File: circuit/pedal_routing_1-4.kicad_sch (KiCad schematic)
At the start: 12 parts, among them U501 CD4051B, U502 CD4051B, U503 CD4051B, U504 CD4051B

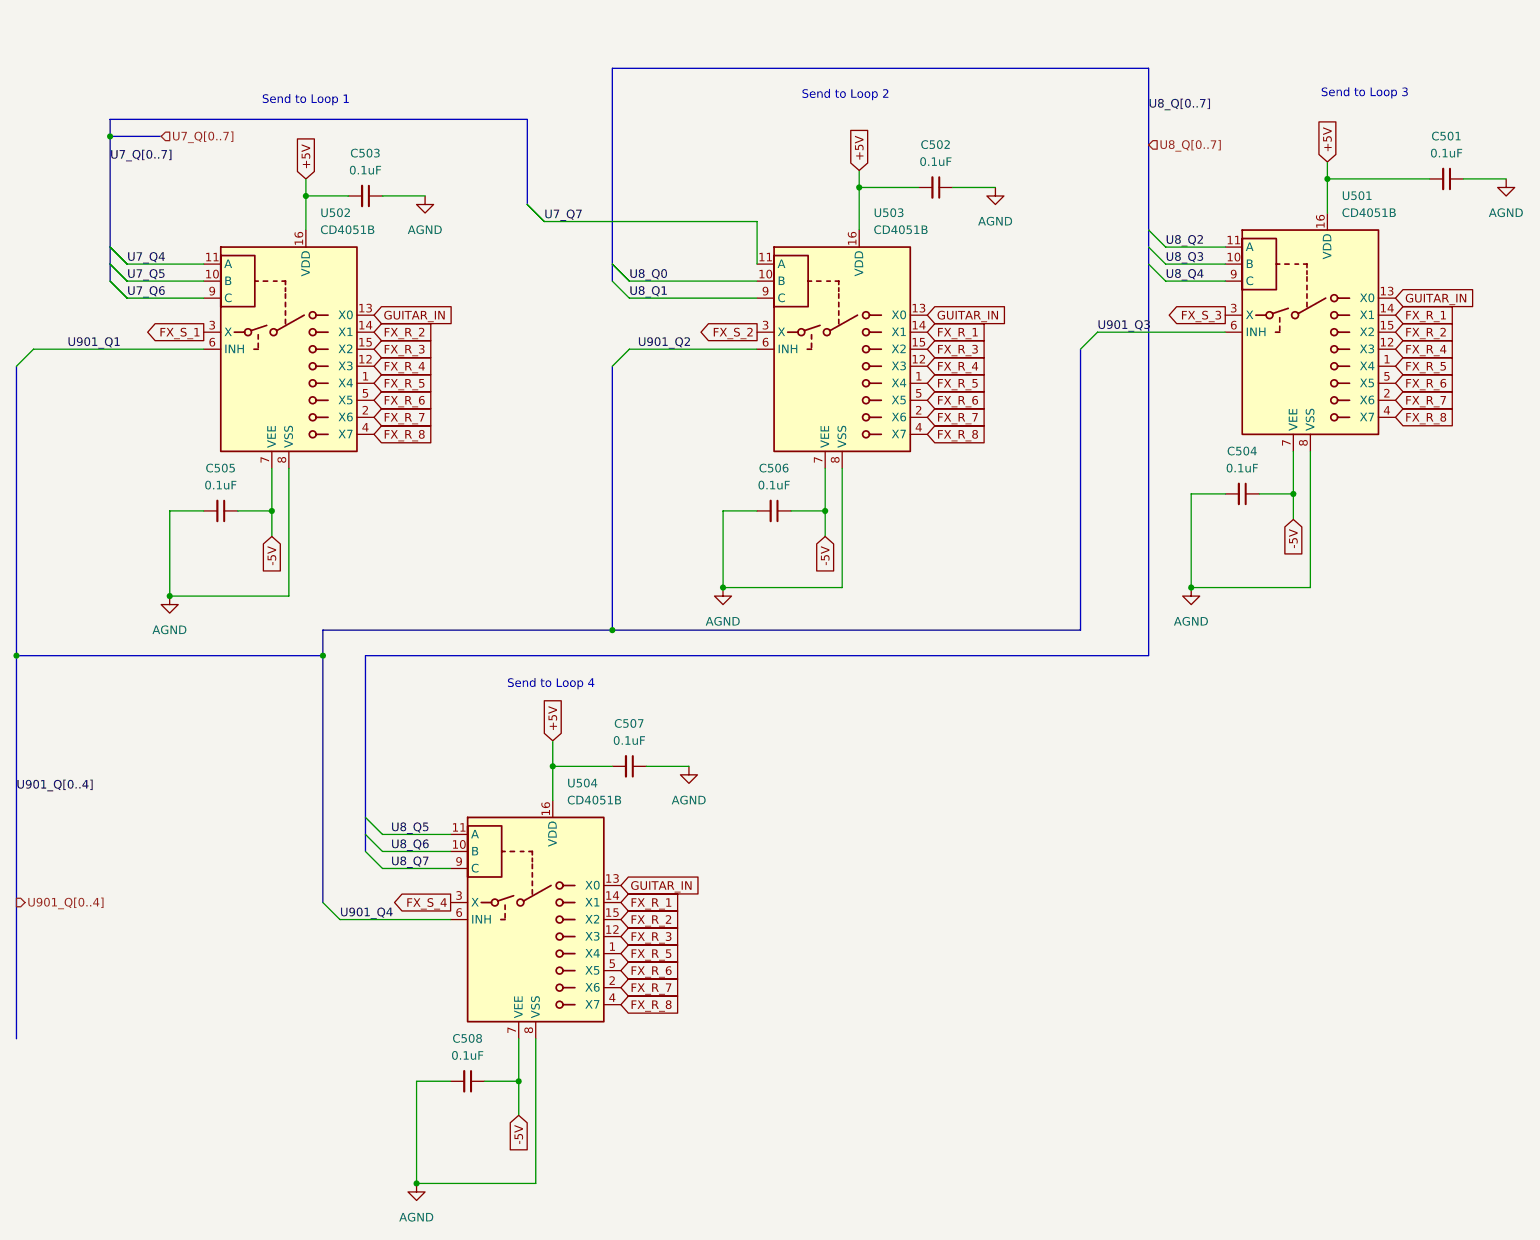
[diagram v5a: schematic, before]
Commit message: Added ferrite beads and tweaked PCB
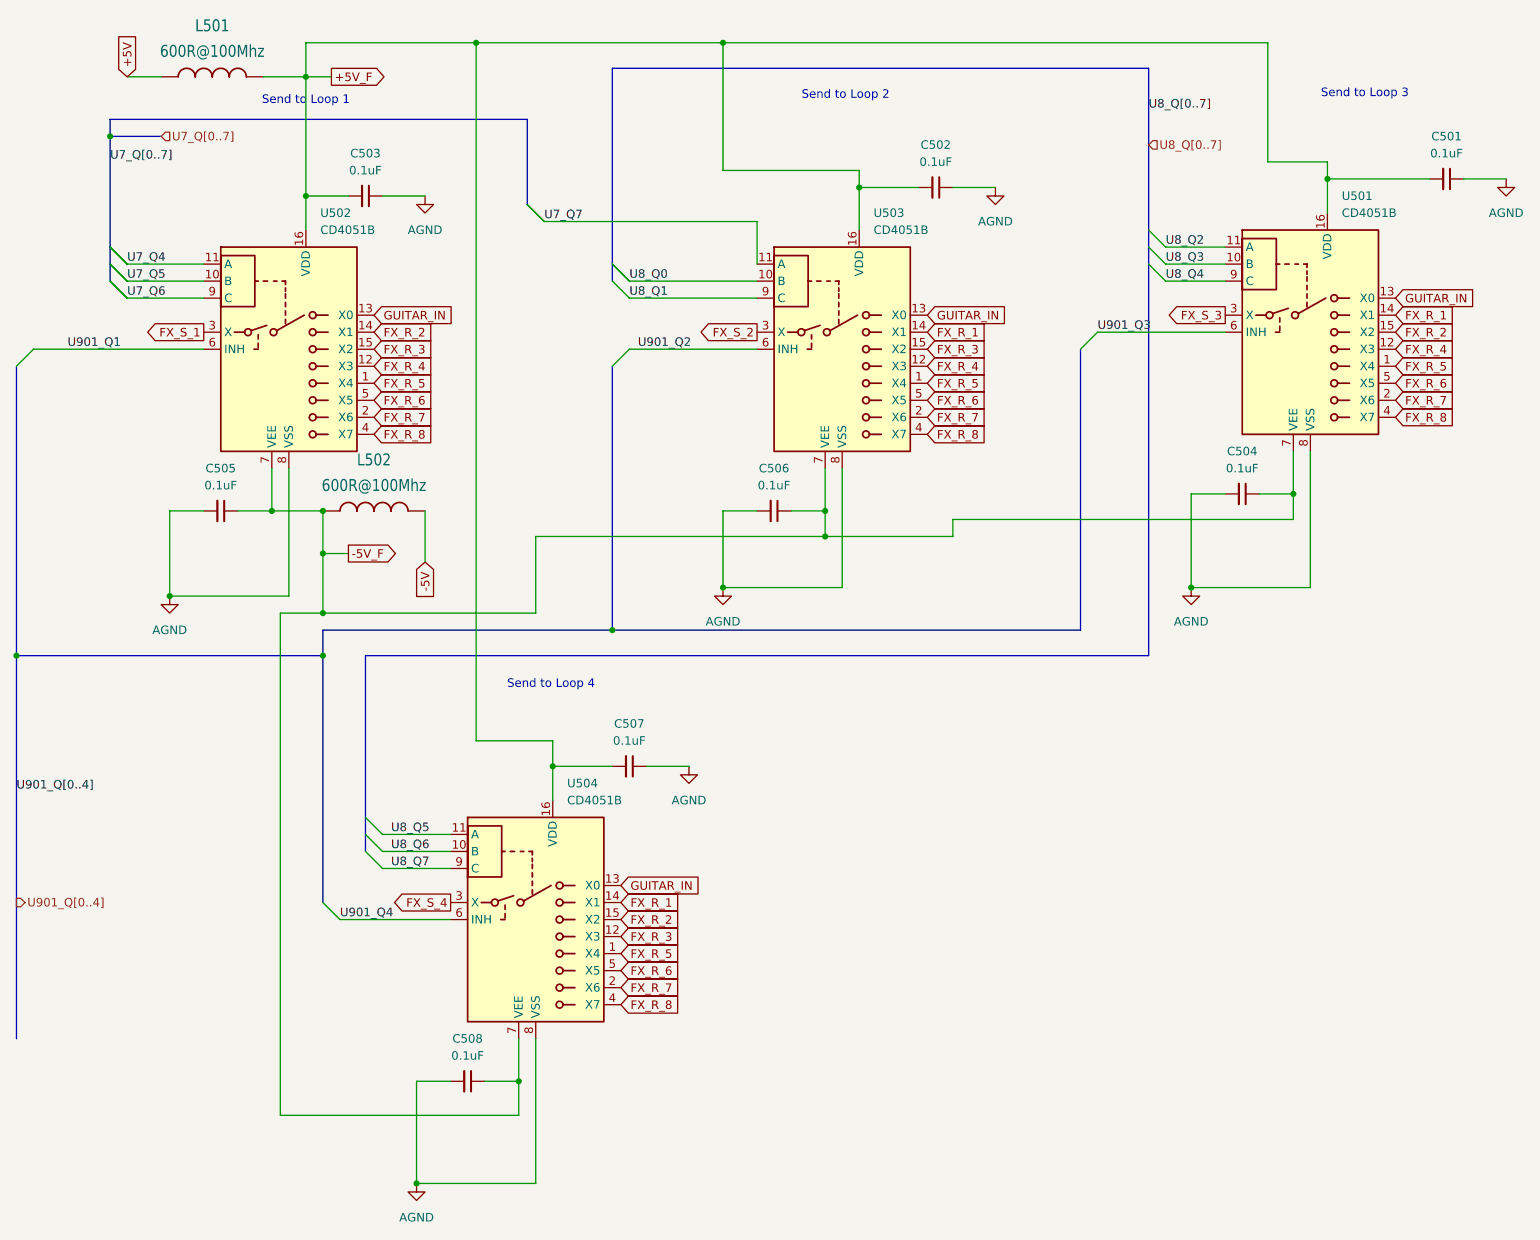
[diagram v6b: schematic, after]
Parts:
- added L501, L502: 600R@100Mhz, WE-UKW:WE-UKW_74275010, symbol WE_UKW:WE-UKW_1SW_74275010
- C501, C502, C503, C504, C505, C506, C507, C508: footprint Capacitor_THT:C_Axial_L3.8mm_D2.6mm_P7.50mm_Horizontal -> Capacitor_THT:C_Disc_D3.0mm_W2.0mm_P2.50mm
- U501, U502, U503, U504: footprint Package_DIP:CERDIP-16_W7.62mm_SideBrazed -> Package_DIP:DIP-16_W7.62mm
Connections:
- net +5V: now also L501.1; no longer C501.2, C502.2, C503.2, C507.2, U501.16 (VDD), U502.16 (VDD), U503.16 (VDD), U504.16 (VDD)
- net -5V: now also L502.2; no longer C504.1, C505.1, C506.1, C508.1, U501.7 (VEE), U502.7 (VEE), U503.7 (VEE), U504.7 (VEE)
- new net +5V_F: C501.2, C502.2, C503.2, C507.2, L501.2, U501.16 (VDD), U502.16 (VDD), U503.16 (VDD), U504.16 (VDD)
- new net -5V_F: C504.1, C505.1, C506.1, C508.1, L502.1, U501.7 (VEE), U502.7 (VEE), U503.7 (VEE), U504.7 (VEE)

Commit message: Circuit tweaks and PCB
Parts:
- C501: renamed from C505; footprint Capacitor_THT:C_Disc_D3.0mm_W2.0mm_P2.50mm -> Capacitor_THT:C_Disc_D5.0mm_W2.5mm_P2.50mm
- C502: renamed from C503; footprint Capacitor_THT:C_Disc_D3.0mm_W2.0mm_P2.50mm -> Capacitor_THT:C_Disc_D5.0mm_W2.5mm_P2.50mm
- C503: renamed from C508; footprint Capacitor_THT:C_Disc_D3.0mm_W2.0mm_P2.50mm -> Capacitor_THT:C_Disc_D5.0mm_W2.5mm_P2.50mm
- C504: renamed from C507; footprint Capacitor_THT:C_Disc_D3.0mm_W2.0mm_P2.50mm -> Capacitor_THT:C_Disc_D5.0mm_W2.5mm_P2.50mm
- C505: renamed from C506; footprint Capacitor_THT:C_Disc_D3.0mm_W2.0mm_P2.50mm -> Capacitor_THT:C_Disc_D5.0mm_W2.5mm_P2.50mm
- C506: renamed from C502; footprint Capacitor_THT:C_Disc_D3.0mm_W2.0mm_P2.50mm -> Capacitor_THT:C_Disc_D5.0mm_W2.5mm_P2.50mm
- C507: renamed from C504; footprint Capacitor_THT:C_Disc_D3.0mm_W2.0mm_P2.50mm -> Capacitor_THT:C_Disc_D5.0mm_W2.5mm_P2.50mm
- C508: renamed from C501; footprint Capacitor_THT:C_Disc_D3.0mm_W2.0mm_P2.50mm -> Capacitor_THT:C_Disc_D5.0mm_W2.5mm_P2.50mm
- renumbered U502 to U501, U504 to U502, U501 to U504

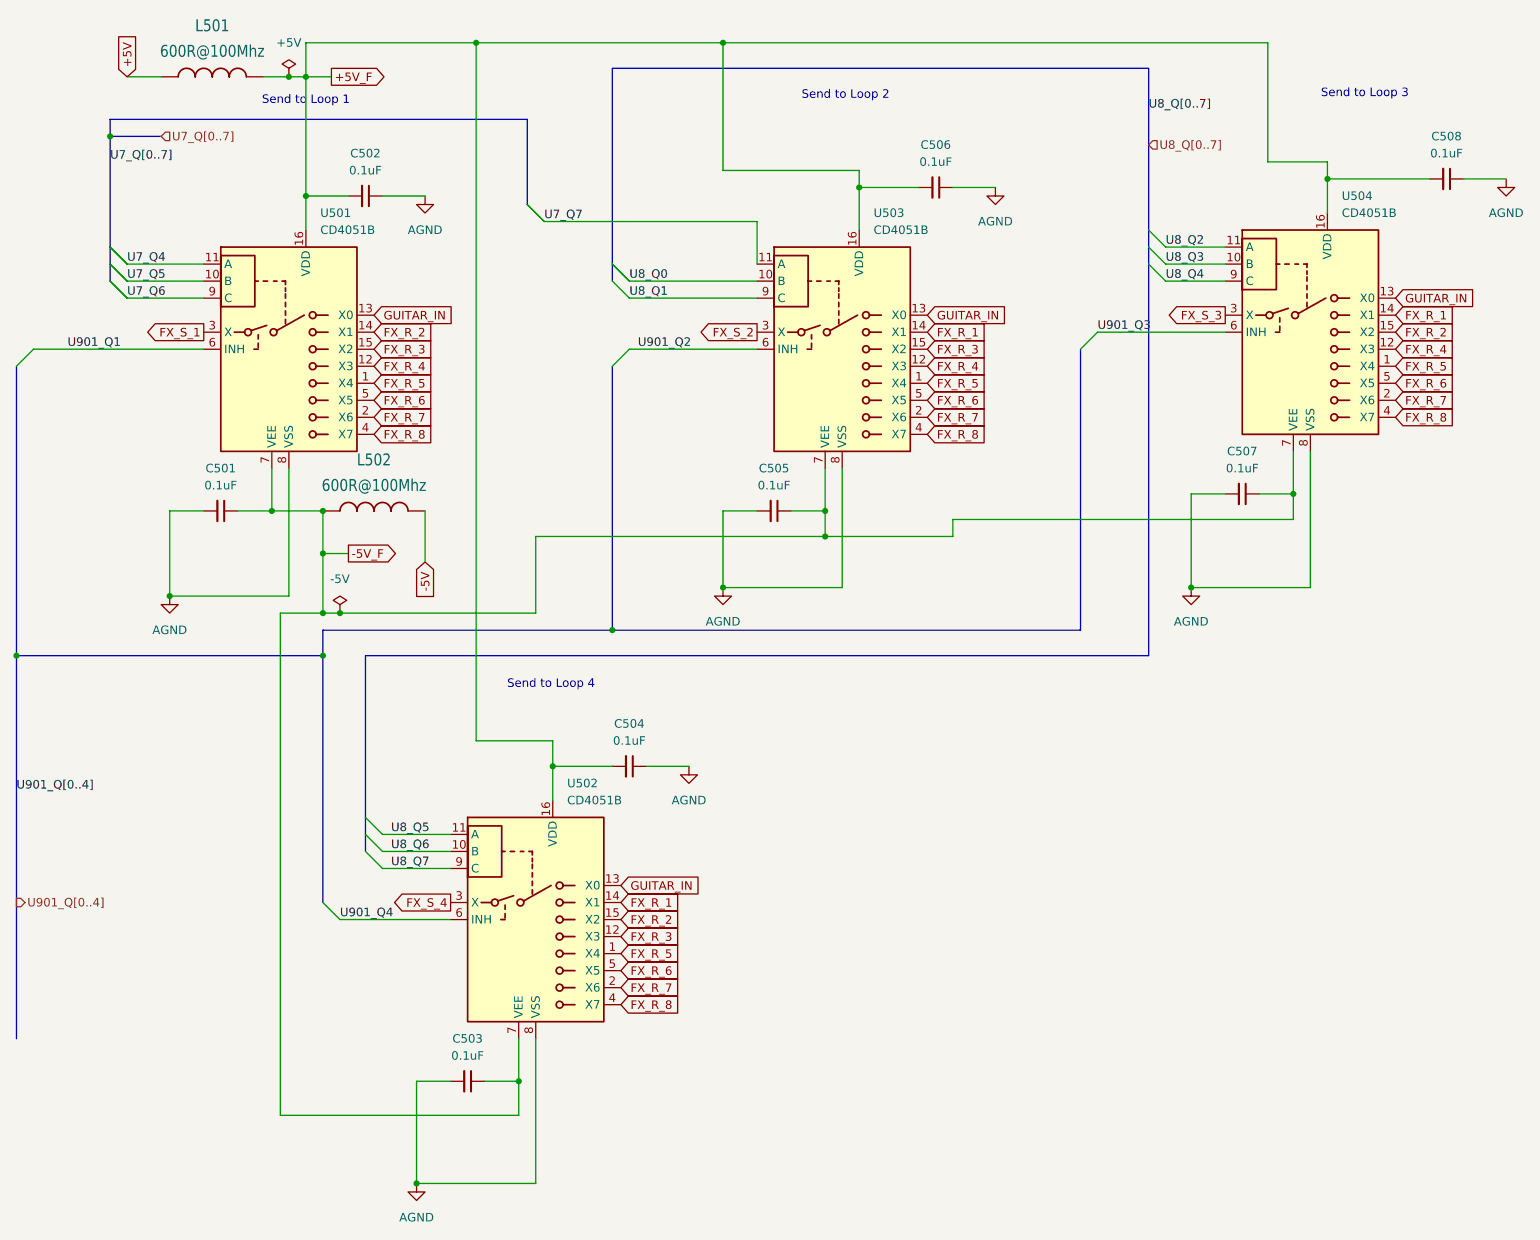
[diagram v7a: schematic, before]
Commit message: Labels for headers on PCB
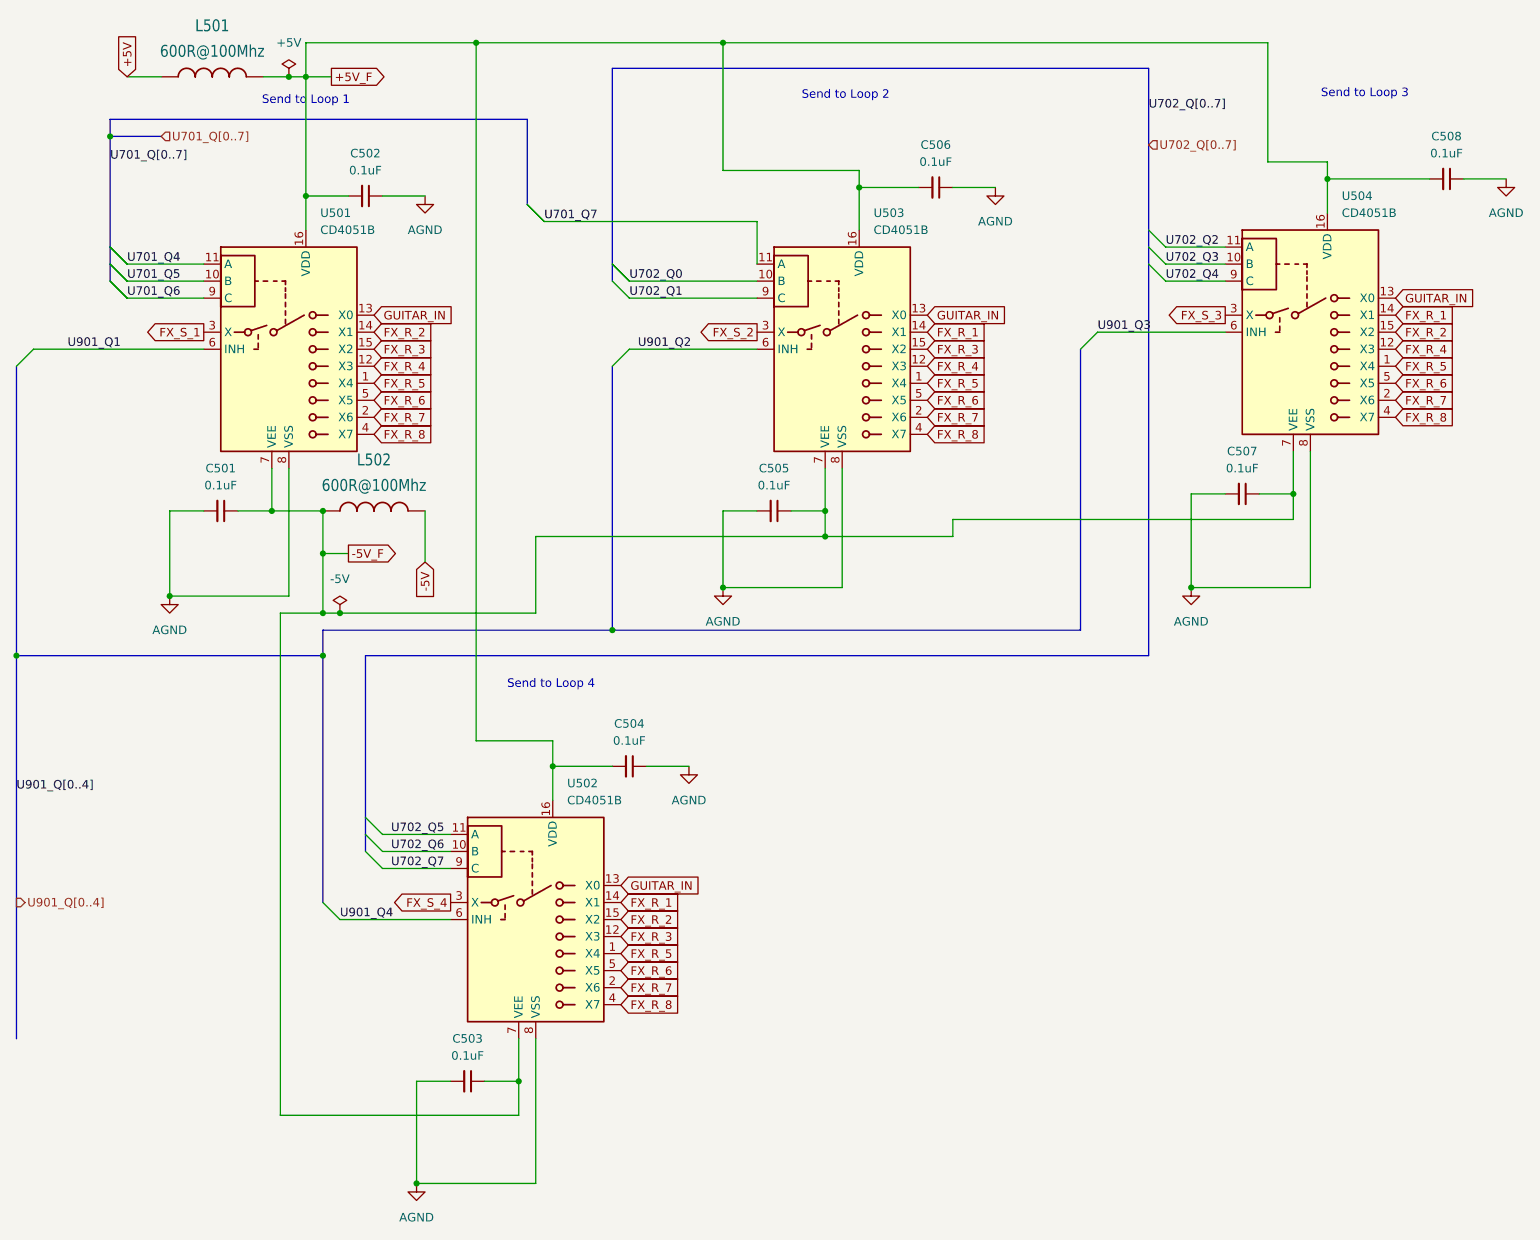
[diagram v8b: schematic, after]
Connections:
- net U7_Q4 renamed U701_Q4
- net U7_Q5 renamed U701_Q5
- net U7_Q6 renamed U701_Q6
- net U7_Q7 renamed U701_Q7
- net U8_Q0 renamed U702_Q0
- net U8_Q1 renamed U702_Q1
- net U8_Q2 renamed U702_Q2
- net U8_Q3 renamed U702_Q3
- net U8_Q4 renamed U702_Q4
- net U8_Q5 renamed U702_Q5
- net U8_Q6 renamed U702_Q6
- net U8_Q7 renamed U702_Q7
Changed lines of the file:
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@@
 		)
 	)
-	(label "U8_Q7"
+	(label "U702_Q7"
 		(at 85.09 137.16 0)
 		(effects
@@
 		)
 	)
-	(label "U8_Q2"
+	(label "U702_Q2"
 		(at 200.66 44.45 0)
 		(effects
@@
 		)
 	)
-	(label "U8_Q[0..7]"
+	(label "U702_Q[0..7]"
 		(at 198.12 24.13 0)
 		(effects
@@
 		)
 	)
-	(label "U7_Q6"
+	(label "U701_Q6"
 		(at 45.72 52.07 0)
 		(effects
@@
 		)
 	)
-	(label "U8_Q6"
+	(label "U702_Q6"
 		(at 85.09 134.62 0)
 		(effects
@@
 		)
 	)
-	(label "U7_Q5"
+	(label "U701_Q5"
 		(at 45.72 49.53 0)
 		(effects
@@
 		)
 	)
-	(label "U7_Q7"
+	(label "U701_Q7"
 		(at 107.95 40.64 0)
 		(effects
@@
 		)
 	)
-	(label "U8_Q4"
+	(label "U702_Q4"
 		(at 200.66 49.53 0)
 		(effects
@@
 		)
 	)
-	(label "U7_Q4"
+	(label "U701_Q4"
 		(at 45.72 46.99 0)
 		(effects
@@
 		)
 	)
-	(label "U8_Q0"
+	(label "U702_Q0"
 		(at 120.65 49.53 0)
 		(effects
@@
 		)
 	)
-	(label "U7_Q[0..7]"
+	(label "U701_Q[0..7]"
 		(at 43.18 31.75 0)
 		(effects
@@
 		)
 	)
-	(label "U8_Q3"
+	(label "U702_Q3"
 		(at 200.66 46.99 0)
 		(effects
@@
 		)
 	)
-	(label "U8_Q1"
+	(label "U702_Q1"
 		(at 120.65 52.07 0)
 		(effects
@@
 		)
 	)
-	(label "U8_Q5"
+	(label "U702_Q5"
 		(at 85.09 132.08 0)
 		(effects
@@
 		)
 	)
-	(hierarchical_label "U8_Q[0..7]"
+	(hierarchical_label "U702_Q[0..7]"
 		(shape input)
 		(at 198.12 29.21 0)
@@
 		)
 	)
-	(hierarchical_label "U7_Q[0..7]"
+	(hierarchical_label "U701_Q[0..7]"
 		(shape input)
 		(at 50.8 27.94 0)
